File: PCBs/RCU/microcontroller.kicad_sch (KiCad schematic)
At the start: 24 parts, among them J200 USB_C_Receptacle_USB2.0, J201 Conn_01x05, U200 STM32G0B1CBT6, U201 USBLC6-2SC6

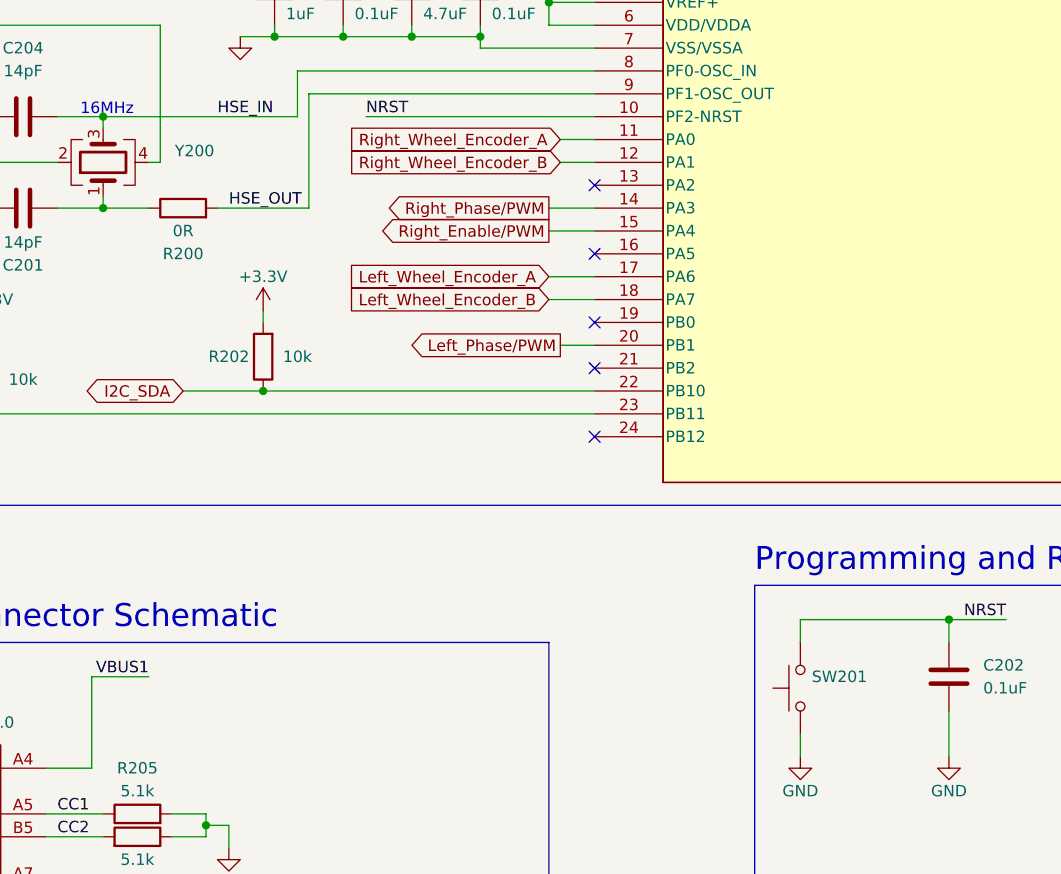
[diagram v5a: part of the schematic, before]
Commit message: Changed Programming/Transcieving button to a slide switch
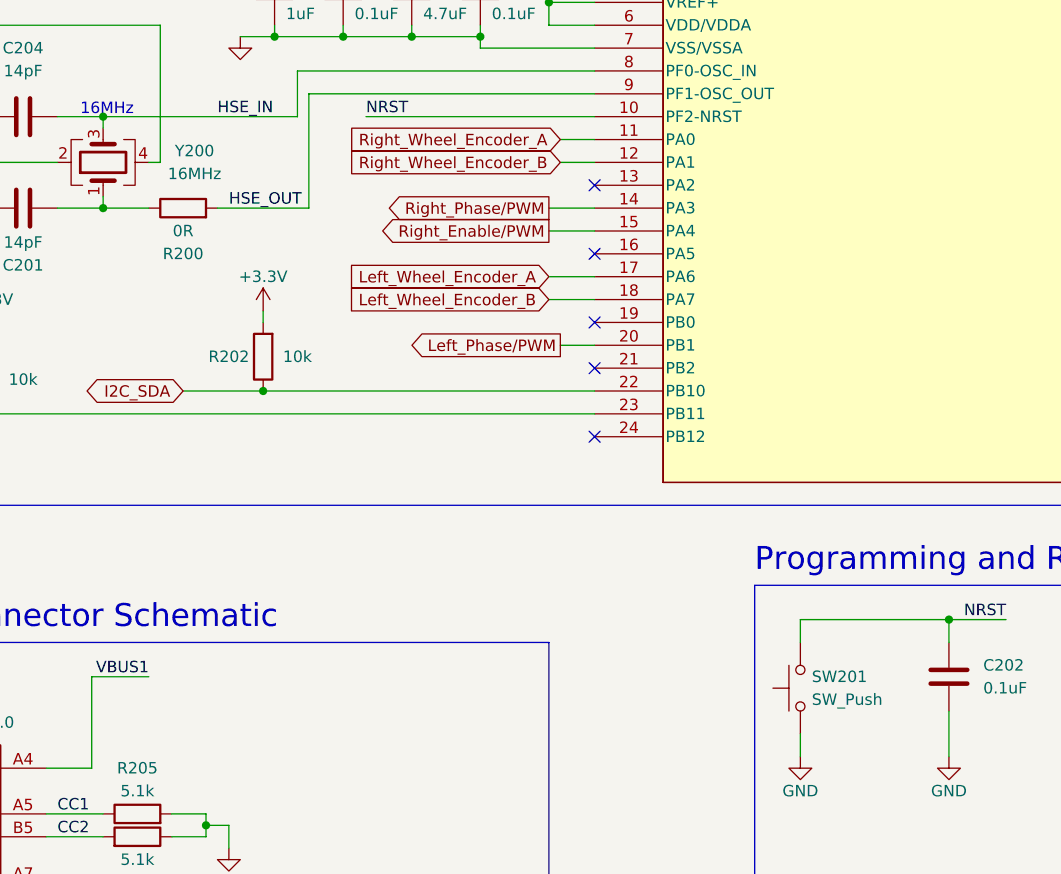
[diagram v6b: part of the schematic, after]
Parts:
- D200, D201, D202, D203: value (none) -> PESD3V3L1BA,115; footprint (none) -> Diode_SMD:D_SOD-323
- SW201: value (none) -> SW_Push; footprint (none) -> Button_Switch_SMD:SW_SPST_B3U-1000P
- Y200: value (none) -> 16MHz; footprint (none) -> Crystal:Crystal_SMD_3225-4Pin_3.2x2.5mm
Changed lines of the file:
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@@
       (effects (font (size 1.27 1.27)) (justify right))
     )
-    (property "Value" "" (id 1) (at 161.29 133.3499 90)
-      (effects (font (size 1.27 1.27)) (justify right))
-    )
-    (property "Footprint" "" (id 2) (at 154.94 132.08 0)
+    (property "Value" "SW_Push" (id 1) (at 161.29 133.3499 90)
+      (effects (font (size 1.27 1.27)) (justify right))
+    )
+    (property "Footprint" "Button_Switch_SMD:SW_SPST_B3U-1000P" (id 2) (at 154.94 132.08 0)
       (effects (font (size 1.27 1.27)) hide)
     )
@@
     (in_bom yes) (on_board yes)
     (property "Reference" "Y200" (id 0) (at 92.71 72.39 90))
-    (property "Value" "" (id 1) (at 92.71 74.93 90))
-    (property "Footprint" "" (id 2) (at 82.55 73.66 0)
+    (property "Value" "16MHz" (id 1) (at 92.71 74.93 90))
+    (property "Footprint" "Crystal:Crystal_SMD_3225-4Pin_3.2x2.5mm" (id 2) (at 82.55 73.66 0)
       (effects (font (size 1.27 1.27)) hide)
     )
@@
       (effects (font (size 1.27 1.27)) (justify right))
     )
-    (property "Value" "" (id 1) (at 226.06 153.67 90)
+    (property "Value" "PESD3V3L1BA,115" (id 1) (at 226.06 153.67 90)
       (effects (font (size 1.27 1.27)) (justify right) hide)
     )
-    (property "Footprint" "" (id 2) (at 224.79 149.86 0)
+    (property "Footprint" "Diode_SMD:D_SOD-323" (id 2) (at 224.79 149.86 0)
       (effects (font (size 1.27 1.27)) hide)
     )
@@
       (effects (font (size 1.27 1.27)) (justify right))
     )
-    (property "Value" "" (id 1) (at 205.74 153.67 90)
+    (property "Value" "PESD3V3L1BA,115" (id 1) (at 205.74 153.67 90)
       (effects (font (size 1.27 1.27)) (justify right) hide)
     )
-    (property "Footprint" "" (id 2) (at 204.47 149.86 0)
+    (property "Footprint" "Diode_SMD:D_SOD-323" (id 2) (at 204.47 149.86 0)
       (effects (font (size 1.27 1.27)) hide)
     )
@@
       (effects (font (size 1.27 1.27)) (justify right))
     )
-    (property "Value" "" (id 1) (at 215.9 153.67 90)
+    (property "Value" "PESD3V3L1BA,115" (id 1) (at 215.9 153.67 90)
       (effects (font (size 1.27 1.27)) (justify right) hide)
     )
-    (property "Footprint" "" (id 2) (at 214.63 149.86 0)
+    (property "Footprint" "Diode_SMD:D_SOD-323" (id 2) (at 214.63 149.86 0)
       (effects (font (size 1.27 1.27)) hide)
     )
@@
       (effects (font (size 1.27 1.27)) (justify right))
     )
-    (property "Value" "" (id 1) (at 224.79 132.08 0)
+    (property "Value" "PESD3V3L1BA,115" (id 1) (at 224.79 132.08 0)
       (effects (font (size 1.27 1.27)) (justify right) hide)
     )
-    (property "Footprint" "" (id 2) (at 227.33 129.54 0)
-      (effects (font (size 1.27 1.27)) hide)
-    )
+    (property "Footprint" "Diode_SMD:D_SOD-323" (id 2) (at 227.33 129.54 0)
+      (effects (font (size 1.27 1.27)) hide)
+    )

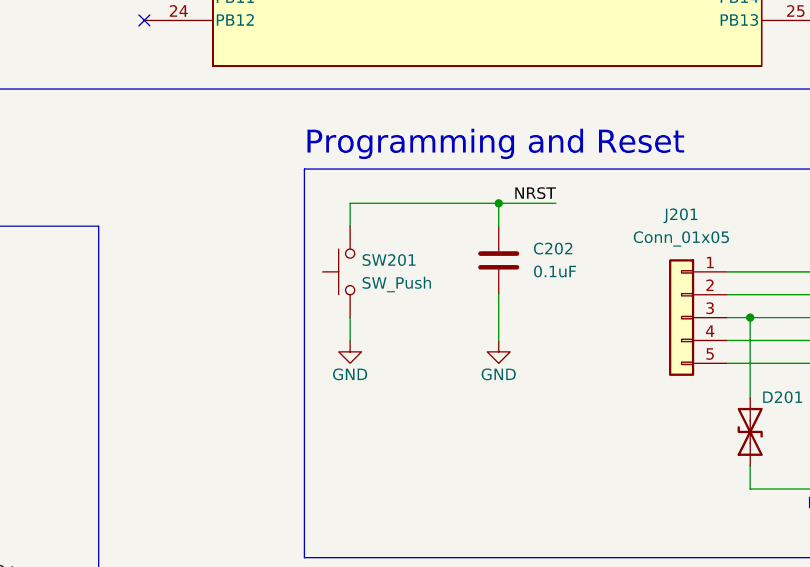
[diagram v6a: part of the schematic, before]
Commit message: Add footprints to leds, fets and push buttons
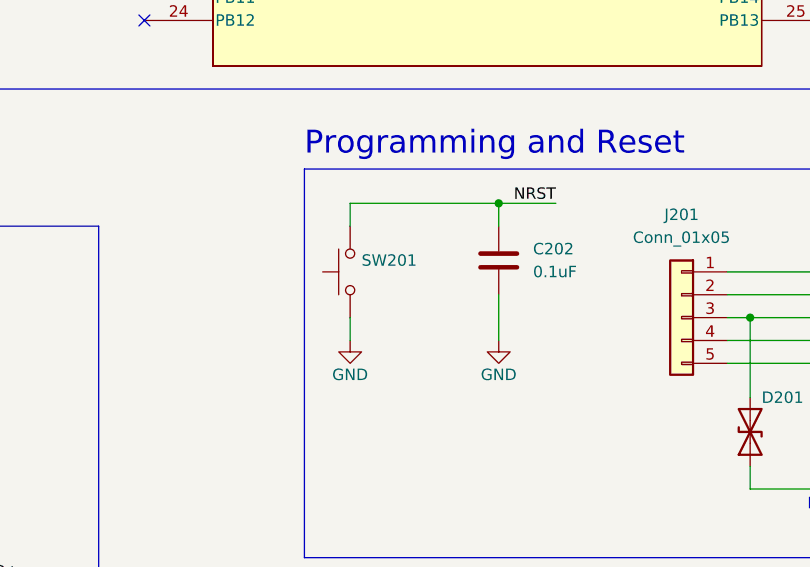
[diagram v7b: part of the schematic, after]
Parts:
- SW201: value SW_Push -> (none); footprint Button_Switch_SMD:SW_SPST_B3U-1000P -> (none)
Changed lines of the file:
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@@
       (effects (font (size 1.27 1.27)) (justify right))
     )
-    (property "Value" "SW_Push" (id 1) (at 161.29 133.3499 90)
+    (property "Value" "" (id 1) (at 161.29 133.3499 90)
       (effects (font (size 1.27 1.27)) (justify right))
     )
-    (property "Footprint" "Button_Switch_SMD:SW_SPST_B3U-1000P" (id 2) (at 154.94 132.08 0)
+    (property "Footprint" "" (id 2) (at 154.94 132.08 0)
       (effects (font (size 1.27 1.27)) hide)
     )

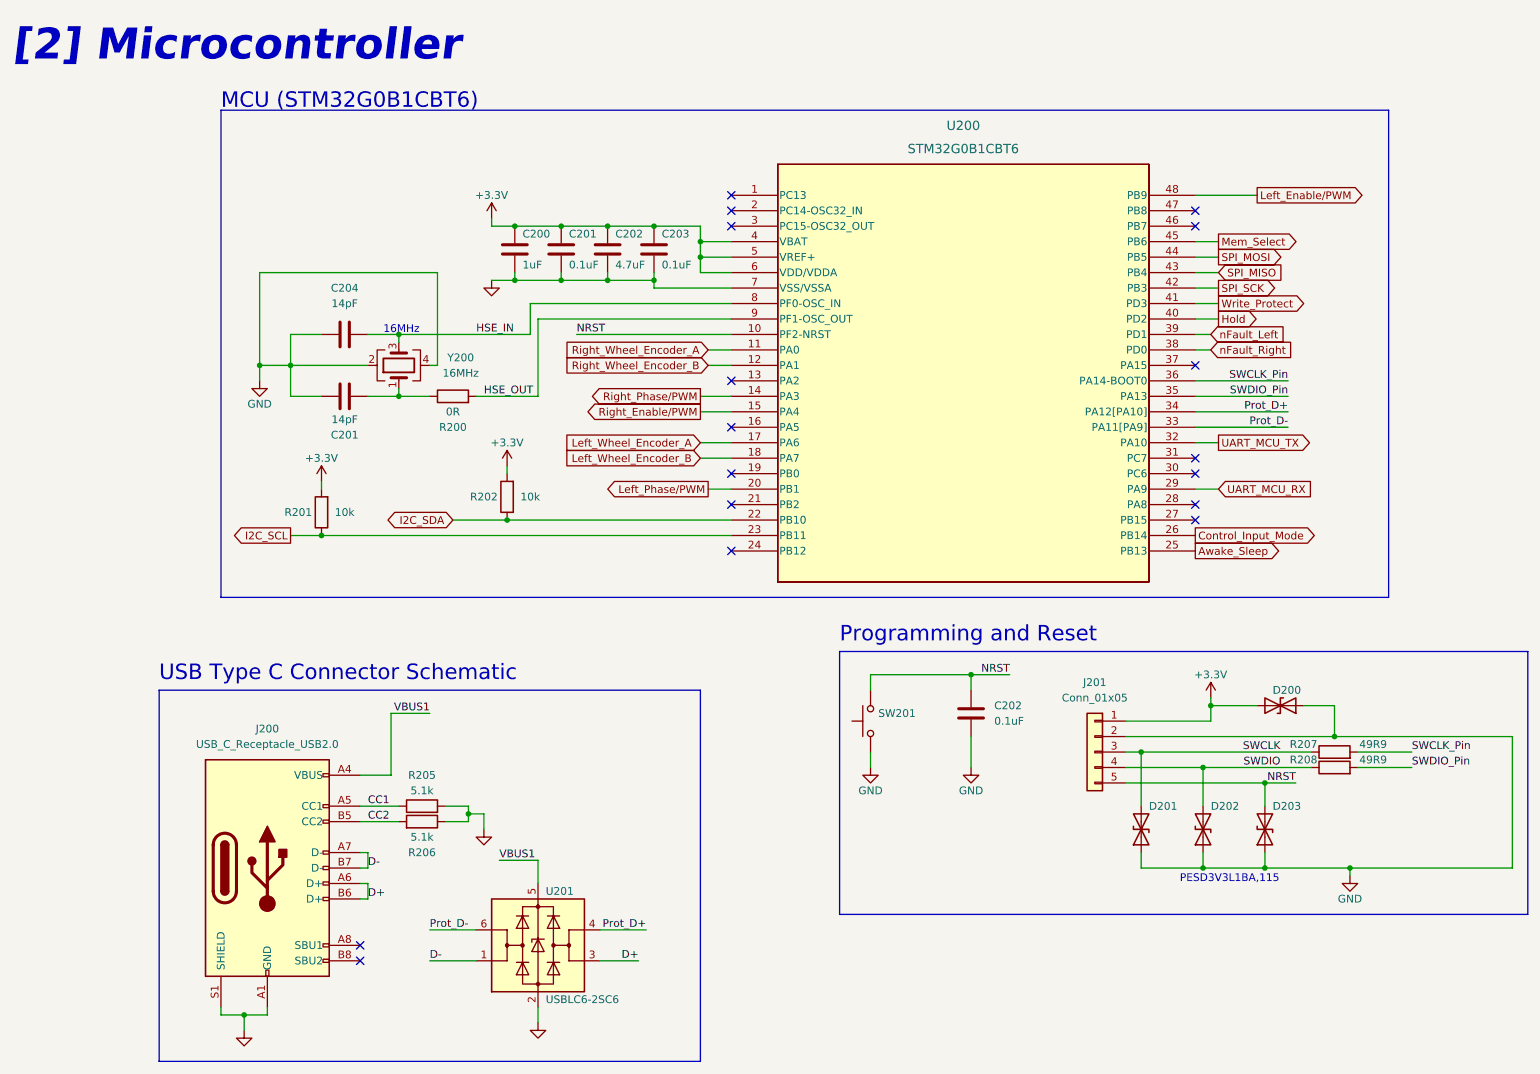
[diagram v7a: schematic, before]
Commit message: Add footrpints to TVS diodes in [3]
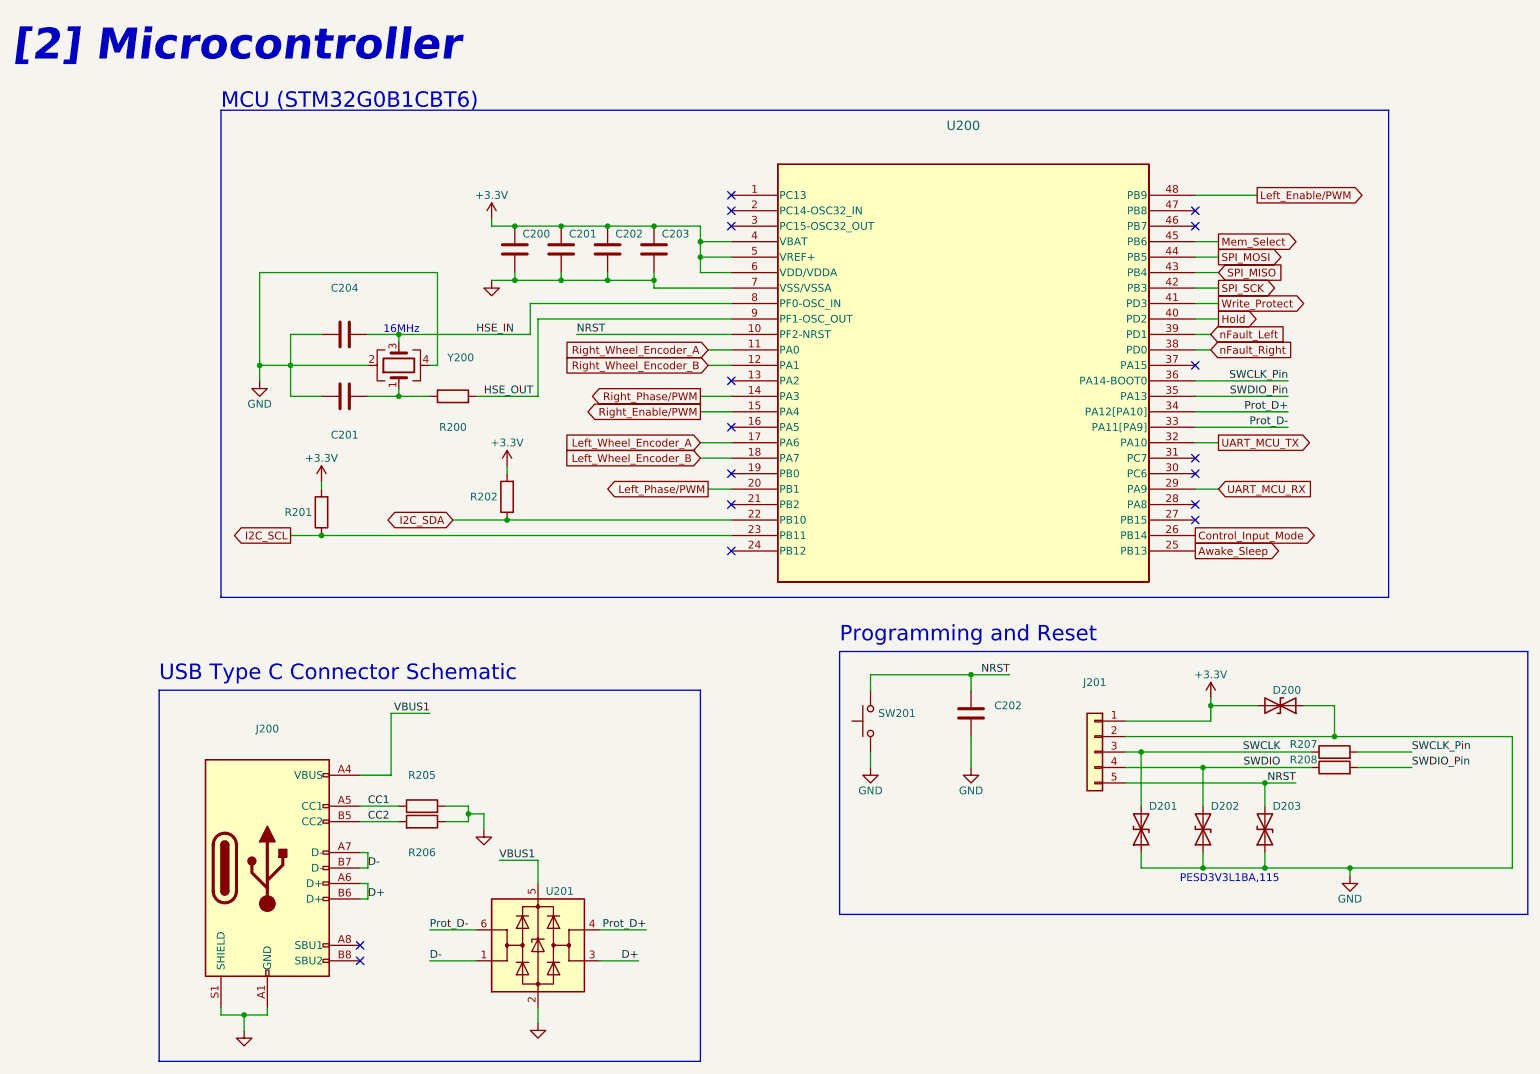
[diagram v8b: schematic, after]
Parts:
- C200: value 1uF -> (none)
- C201, C204: value 14pF -> (none)
- C201, C202, C203: value 0.1uF -> (none)
- C202: value 4.7uF -> (none)
- D200, D201, D202, D203: value PESD3V3L1BA,115 -> (none); footprint Diode_SMD:D_SOD-323 -> (none)
- J200: value USB_C_Receptacle_USB2.0 -> (none); footprint Connector_USB:USB_C_Receptacle_HRO_TYPE-C-31-M-12 -> (none)
- J201: value Conn_01x05 -> (none); footprint Connector_PinHeader_2.54mm:PinHeader_1x05_P2.54mm_Vertical -> (none)
- R200: value 0R -> (none)
- R201, R202: value 10k -> (none)
- R205, R206: value 5.1k -> (none)
- R207, R208: value 49R9 -> (none)
- U200: value STM32G0B1CBT6 -> (none); footprint Package_QFP:LQFP-48-1EP_7x7mm_P0.5mm_EP3.6x3.6mm -> (none)
- U201: value USBLC6-2SC6 -> (none); footprint Package_TO_SOT_SMD:SOT-23-6 -> (none)
- Y200: value 16MHz -> (none); footprint Crystal:Crystal_SMD_3225-4Pin_3.2x2.5mm -> (none)
